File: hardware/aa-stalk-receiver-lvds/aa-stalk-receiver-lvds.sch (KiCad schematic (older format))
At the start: 71 parts, among them CN1 Conn_01x02, CN2 Conn_01x04, CN3 6P6C, CN4 Conn_01x03, CN5 Conn_01x02, CN6 Conn_01x02, CN7 Conn_01x02, CN8 Conn_01x02, Q1 MMBTA06, Q2 MCH3484, Q3 MCH3484, U1 AZ1117-5.0, U2 MIC5504-3.3YM5, U3 LM4562, U4 FIN1028, U5 MC3486N

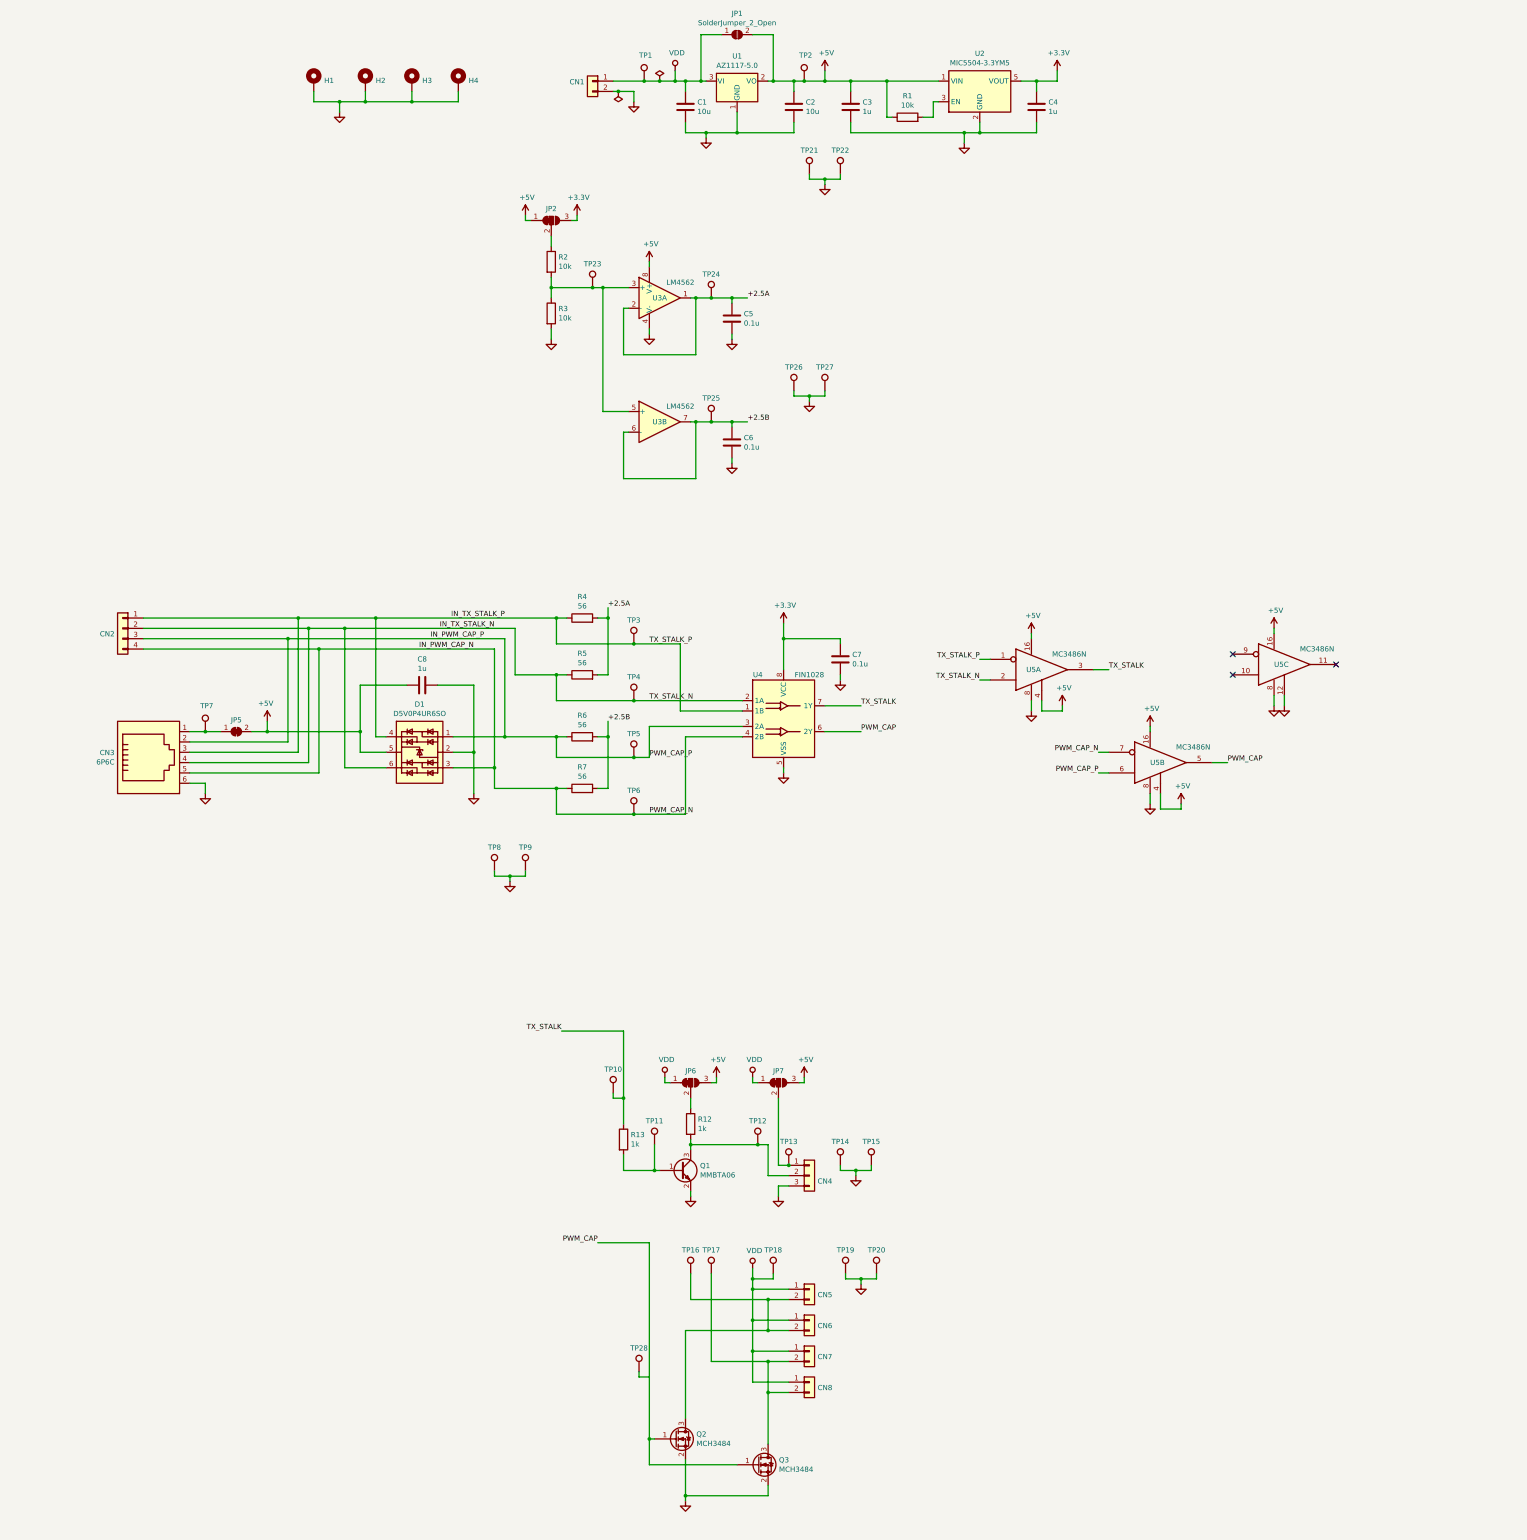
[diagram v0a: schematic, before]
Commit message: Updates to schematic and layout -- remove test points, add jumpers, iterate layout
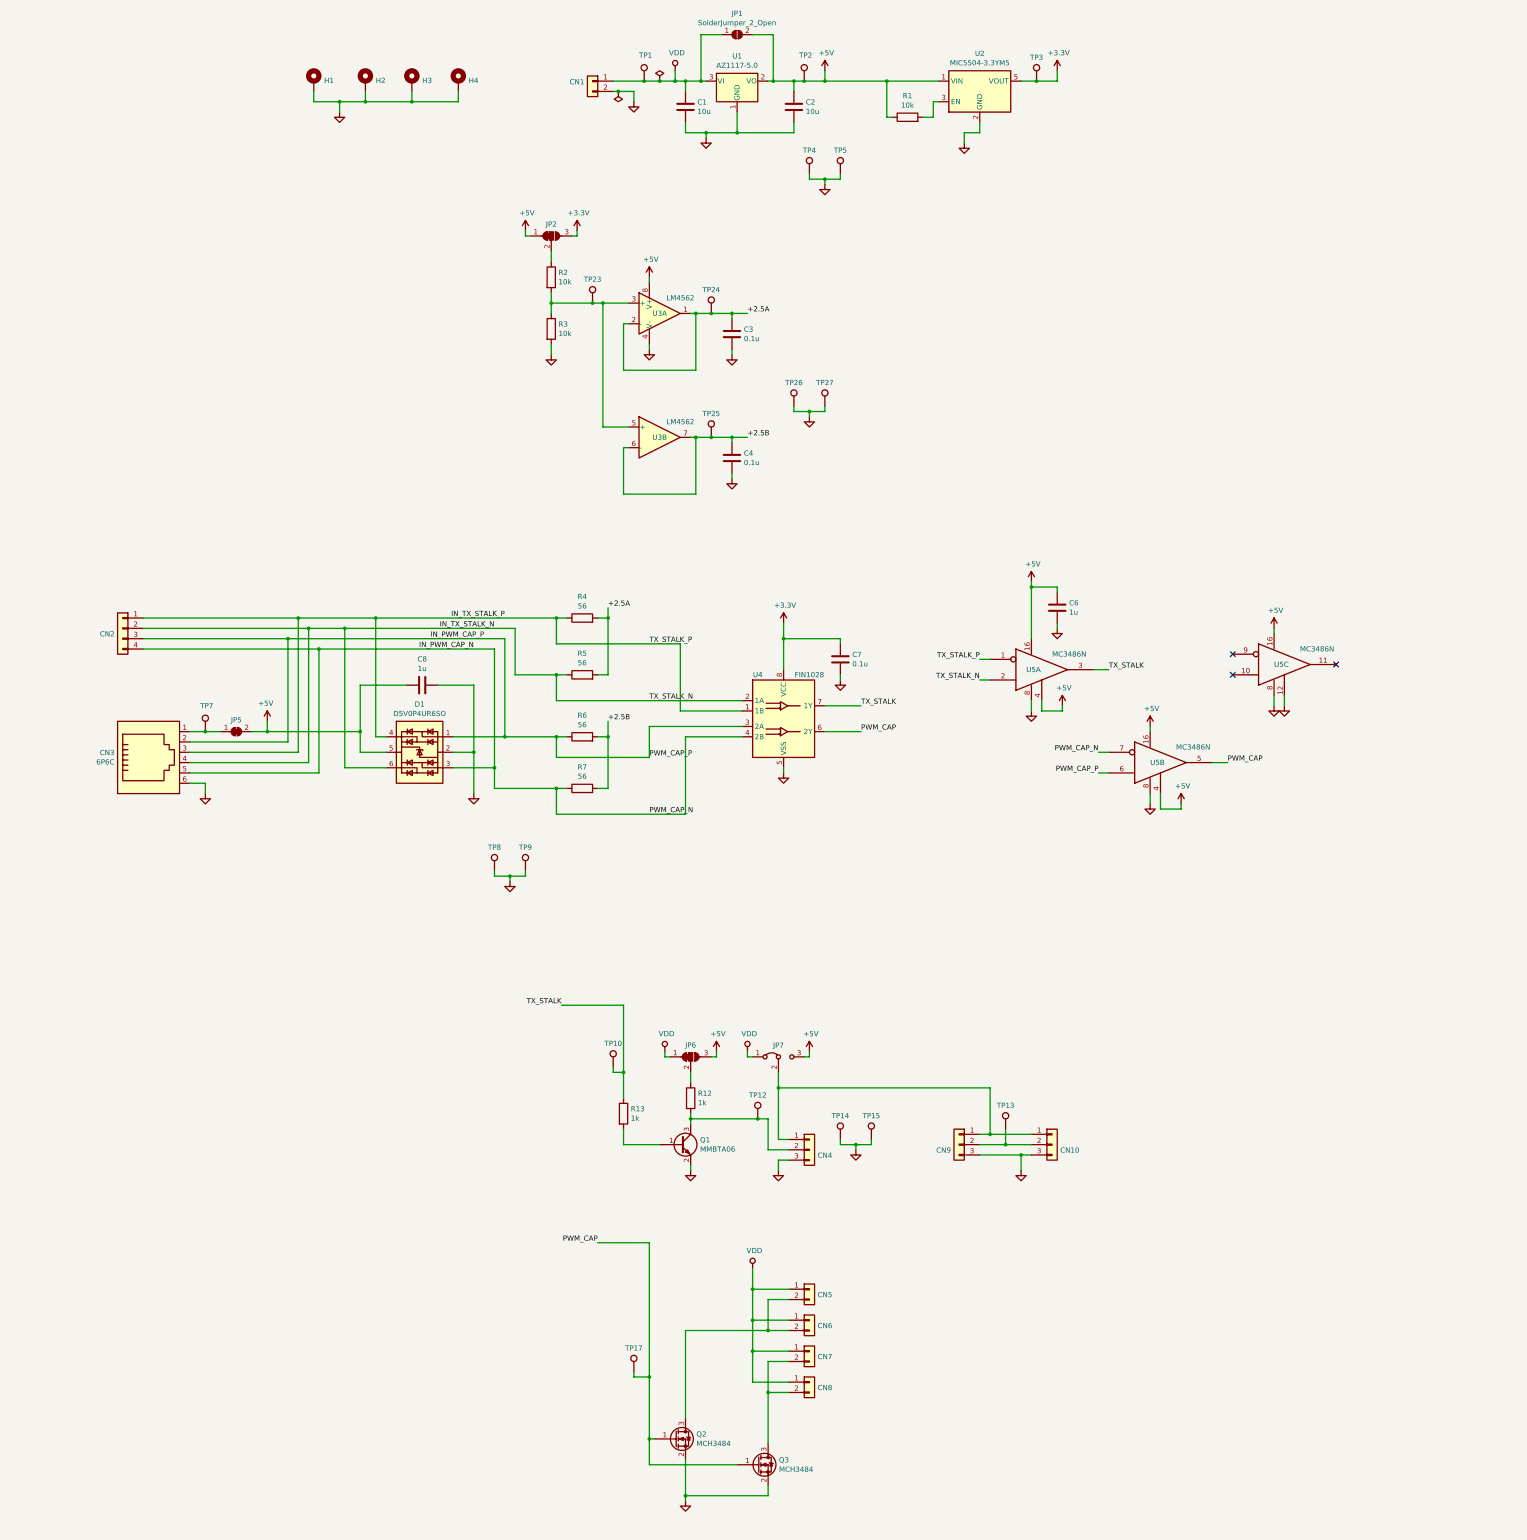
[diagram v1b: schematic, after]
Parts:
- removed C3: 1u, Capacitor_SMD:C_0805_2012Metric, symbol Device:C
- removed JP7: SolderJumper_3_Bridged12, Jumper:SolderJumper-3_P1.3mm_Bridged12_RoundedPad1.0x1.5mm, symbol Jumper:SolderJumper_3_Bridged12
- removed TP11, TP16, TP17, TP18, TP19, TP20, TP3, TP4, TP6: TestPoint, TestPoint:TestPoint_THTPad_D2.0mm_Drill1.0mm, symbol Connector:TestPoint
- added CN10, CN9: Conn_01x03, Connector_PinHeader_2.54mm:PinHeader_1x03_P2.54mm_Vertical, symbol Connector_Generic:Conn_01x03
- added JP7: Jumper_3_Bridged12, Connector_PinHeader_2.54mm:PinHeader_1x03_P2.54mm_Vertical, symbol Jumper:Jumper_3_Bridged12
- renumbered C5 to C3, C6 to C4, C4 to C6, TP28 to TP17, TP21 to TP3, TP22 to TP4
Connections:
- net +3V3: now also TP3.1; no longer C6.1
- net +5V: now also C6.1, JP7.3 (B)
- net GND: now also TP5.1, CN10.3 (Pin_3), CN9.3 (Pin_3); no longer TP3.1
- net IN_PWM_CAP_P: no longer TP5.1
- net PWM_CAP: now also TP17.1
- net VDD: now also JP7.1 (A)
- net at CN4.1 (Pin_1): now also CN10.1 (Pin_1), CN9.1 (Pin_1), JP7.2 (C); no longer TP13.1
- new net: CN10.2 (Pin_2), CN9.2 (Pin_2), TP13.1
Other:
- moved on the sheet: C3, C4, C6, CN4, JP2, JP6, Q1, R12, R13, R2, R3, TP10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

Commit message: Latest stalk receiver design -- many tweaks, layout V0 probably done
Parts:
- added C5, C9: 10u, Capacitor_SMD:C_0805_2012Metric, symbol Device:C
- Q1: value MMBTA06 -> KST10
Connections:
- net GND: now also C5.2, C9.2
- net VDD: now also C5.1, C9.1; no longer JP6.1 (A)
- net at CN10.1 (Pin_1), CN4.1 (Pin_1), CN9.1 (Pin_1)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: now also JP6.1 (A)
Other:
- moved on the sheet: Q2, Q3
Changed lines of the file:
@@
 L Device:Q_NMOS_GSD Q2
 U 1 1 5D1BFE0F
-P 10150 14900
-F 0 "Q2" H 10355 14946 50  0000 L CNN
-F 1 "MCH3484" H 10355 14855 50  0000 L CNN
-F 2 "Package_TO_SOT_SMD:SOT-323_SC-70" H 10350 15000 50  0001 C CNN
-F 3 "~" H 10150 14900 50  0001 C CNN
-	1    10150 14900
+P 10150 14700
+F 0 "Q2" H 10355 14746 50  0000 L CNN
+F 1 "MCH3484" H 10355 14655 50  0000 L CNN
+F 2 "Package_TO_SOT_SMD:SOT-323_SC-70" H 10350 14800 50  0001 C CNN
+F 3 "~" H 10150 14700 50  0001 C CNN
+	1    10150 14700
 	1    0    0    -1
 $EndComp
@@
 L power:GND #PWR030
 U 1 1 5D1C09BE
-P 10250 15500
-F 0 "#PWR030" H 10250 15250 50  0001 C CNN
-F 1 "GND" H 10255 15327 50  0001 C CNN
-F 2 "" H 10250 15500 50  0001 C CNN
-F 3 "" H 10250 15500 50  0001 C CNN
-	1    10250 15500
+P 10250 15700
+F 0 "#PWR030" H 10250 15450 50  0001 C CNN
+F 1 "GND" H 10255 15527 50  0001 C CNN
+F 2 "" H 10250 15700 50  0001 C CNN
+F 3 "" H 10250 15700 50  0001 C CNN
+	1    10250 15700
 	-1   0    0    -1
 $EndComp
@@
 P 10200 12050
 F 0 "Q1" H 10391 12096 50  0000 L CNN
-F 1 "MMBTA06" H 10391 12005 50  0000 L CNN
+F 1 "KST10" H 10391 12005 50  0000 L CNN
 F 2 "Package_TO_SOT_SMD:SOT-23" H 10400 12150 50  0001 C CNN
 F 3 "~" H 10200 12050 50  0001 C CNN
@@
 L power:+5V #PWR022
 U 1 1 5CE1E945
-P 10550 11150
-F 0 "#PWR022" H 10550 11000 50  0001 C CNN
-F 1 "+5V" H 10565 11323 50  0000 C CNN
-F 2 "" H 10550 11150 50  0001 C CNN
-F 3 "" H 10550 11150 50  0001 C CNN
-	1    10550 11150
-	1    0    0    -1
-$EndComp
-$Comp
-L power:VDD #PWR021
-U 1 1 5CE20E4F
 P 10050 11150
-F 0 "#PWR021" H 10050 11000 50  0001 C CNN
-F 1 "VDD" H 10067 11323 50  0000 C CNN
+F 0 "#PWR022" H 10050 11000 50  0001 C CNN
+F 1 "+5V" H 10065 11323 50  0000 C CNN
 F 2 "" H 10050 11150 50  0001 C CNN
 F 3 "" H 10050 11150 50  0001 C CNN
 	1    10050 11150
-	1    0    0    -1
+	-1   0    0    -1
 $EndComp
 $Comp
@@
 F 3 "~" H 10300 11200 50  0001 C CNN
 	1    10300 11200
-	1    0    0    -1
-$EndComp
-Wire Wire Line
-	10050 11150 10050 11200
-Wire Wire Line
-	10050 11200 10100 11200
-Wire Wire Line
-	10500 11200 10550 11200
-Wire Wire Line
-	10550 11200 10550 11150
+	-1   0    0    -1
+$EndComp
+Wire Wire Line
+	10100 11200 10050 11200
+Wire Wire Line
+	10050 11200 10050 11150
 Wire Wire Line
 	10300 11350 10300 11450
@@
 	11250 13850 11050 13850
 Connection ~ 11050 13850
-Wire Wire Line
-	10250 15100 10250 15450
 $Comp
 L Connector:TestPoint TP12
@@
 $EndComp
 Wire Wire Line
-	9900 14900 9950 14900
+	9900 14700 9950 14700
 $Comp
 L Device:Q_NMOS_GSD Q3
 U 1 1 5D012D13
-P 10950 15150
-F 0 "Q3" H 11155 15196 50  0000 L CNN
-F 1 "MCH3484" H 11155 15105 50  0000 L CNN
-F 2 "Package_TO_SOT_SMD:SOT-323_SC-70" H 11150 15250 50  0001 C CNN
-F 3 "~" H 10950 15150 50  0001 C CNN
-	1    10950 15150
-	1    0    0    -1
-$EndComp
-Wire Wire Line
-	10250 15450 11050 15450
-Wire Wire Line
-	11050 15450 11050 15350
-Connection ~ 10250 15450
-Wire Wire Line
-	10250 15450 10250 15500
-Wire Wire Line
-	10750 15150 9900 15150
-Wire Wire Line
-	9900 15150 9900 14900
-Connection ~ 9900 14900
-Wire Wire Line
-	11050 14450 11050 14950
-Wire Wire Line
-	10250 14700 10250 13850
+P 10950 15350
+F 0 "Q3" H 11155 15396 50  0000 L CNN
+F 1 "MCH3484" H 11155 15305 50  0000 L CNN
+F 2 "Package_TO_SOT_SMD:SOT-323_SC-70" H 11150 15450 50  0001 C CNN
+F 3 "~" H 10950 15350 50  0001 C CNN
+	1    10950 15350
+	1    0    0    -1
+$EndComp
+Wire Wire Line
+	10250 15600 11050 15600
+Wire Wire Line
+	11050 15600 11050 15550
+Connection ~ 10250 15600
+Wire Wire Line
+	11050 14450 11050 15150
+Wire Wire Line
+	10250 14500 10250 13850
 Wire Wire Line
 	10250 13850 11050 13850
@@
 	11450 11200 11450 11150
 Wire Wire Line
-	11150 11350 11150 11500
+	11150 11350 11150 11400
 Wire Wire Line
 	10200 7200 10200 7850
@@
 Connection ~ 9900 14300
 Wire Wire Line
-	9900 14300 9900 14900
+	9900 14300 9900 14400
 Wire Wire Line
 	11600 1750 12200 1750
@@
 	1    0    0    -1
 $EndComp
+$Comp
+L Device:C C5
+U 1 1 5D0E86A8
+P 9550 14800
+F 0 "C5" H 9665 14846 50  0000 L CNN
+F 1 "10u" H 9665 14755 50  0000 L CNN
+F 2 "Capacitor_SMD:C_0805_2012Metric" H 9588 14650 50  0001 C CNN
+F 3 "~" H 9550 14800 50  0001 C CNN
+	1    9550 14800
+	1    0    0    -1
+$EndComp
+$Comp
+L Device:C C9
+U 1 1 5D0E98B7
+P 11650 15400
+F 0 "C9" H 11765 15446 50  0000 L CNN
+F 1 "10u" H 11765 15355 50  0000 L CNN
+F 2 "Capacitor_SMD:C_0805_2012Metric" H 11688 15250 50  0001 C CNN
+F 3 "~" H 11650 15400 50  0001 C CNN
+	1    11650 15400
+	1    0    0    -1
+$EndComp
+Wire Wire Line
+	9900 14400 10600 14400
+Wire Wire Line
+	10600 14400 10600 15350
+Wire Wire Line
+	10600 15350 10750 15350
+Connection ~ 9900 14400
+Wire Wire Line
+	9900 14400 9900 14700
+$Comp
+L power:VDD #PWR0111
+U 1 1 5D122E43
+P 9550 14600
+F 0 "#PWR0111" H 9550 14450 50  0001 C CNN
+F 1 "VDD" H 9567 14773 50  0000 C CNN
+F 2 "" H 9550 14600 50  0001 C CNN
+F 3 "" H 9550 14600 50  0001 C CNN
+	1    9550 14600
+	1    0    0    -1
+$EndComp
+$Comp
+L power:VDD #PWR0112
+U 1 1 5D122ED6
+P 11650 15200
+F 0 "#PWR0112" H 11650 15050 50  0001 C CNN
+F 1 "VDD" H 11667 15373 50  0000 C CNN
+F 2 "" H 11650 15200 50  0001 C CNN
+F 3 "" H 11650 15200 50  0001 C CNN
+	1    11650 15200
+	1    0    0    -1
+$EndComp
+Wire Wire Line
+	11650 15200 11650 15250
+Wire Wire Line
+	9550 14600 9550 14650
+Wire Wire Line
+	9550 14950 9550 15000
+Wire Wire Line
+	9550 15000 10250 15000
+Wire Wire Line
+	10250 14900 10250 15000
+Connection ~ 10250 15000
+Wire Wire Line
+	10250 15000 10250 15600
+Wire Wire Line
+	11050 15600 11650 15600
+Wire Wire Line
+	11650 15550 11650 15600
+Wire Wire Line
+	10250 15600 10250 15700
+Connection ~ 11050 15600
+Wire Wire Line
+	10650 11200 10650 11400
+Wire Wire Line
+	10650 11400 11150 11400
+Wire Wire Line
+	10500 11200 10650 11200
+Connection ~ 11150 11400
+Wire Wire Line
+	11150 11400 11150 11500
 $EndSCHEMATC
